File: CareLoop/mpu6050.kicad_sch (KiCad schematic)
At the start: 6 parts, among them U3 MPU-6050

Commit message: updated version
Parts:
- C11: value 10n -> 100n
- renumbered C12 to C99, JP2 to JP2_MPU2
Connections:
- net GND: now also C11.1, C13.1, C99.1; no longer C11.2, C13.2, C99.2, JP2_MPU2.1 (A)
- net at U3.13 (VDD): now also C11.2, C99.2, JP2_MPU2.1 (A), U3.8 (VLOGIC); no longer C99.1
- net at U3.20 (CPOUT): now also C13.2; no longer C13.1
- net INT renamed INT_MPU
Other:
- moved on the sheet: C11, C13, C14, C99, JP2_MPU2

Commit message: WP: update Schematics
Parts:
- C11: value 100n -> 10n
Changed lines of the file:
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@@
 	)
 	(junction
-		(at 118.11 99.06)
+		(at 161.29 109.22)
 		(diameter 0)
 		(color 0 0 0 0)
@@
 	(wire
 		(pts
+			(xy 113.03 119.38) (xy 161.29 119.38)
+		)
+		(stroke
+			(width 0)
+			(type default)
+		)
+	)
+	(wire
+		(pts
 			(xy 157.48 63.5) (xy 157.48 60.96)
 		)
@@
 	(wire
 		(pts
+			(xy 118.11 111.76) (xy 139.7 111.76)
+		)
+		(stroke
+			(width 0)
+			(type default)
+		)
+	)
+	(wire
+		(pts
+			(xy 121.92 60.96) (xy 137.16 60.96)
+		)
+		(stroke
+			(width 0)
+			(type default)
+		)
+	)
+	(wire
+		(pts
+			(xy 137.16 60.96) (xy 137.16 73.66)
+		)
+		(stroke
+			(width 0)
+			(type default)
+		)
+	)
+	(wire
+		(pts
+			(xy 167.64 109.22) (xy 167.64 111.76)
+		)
+		(stroke
+			(width 0)
+			(type default)
+		)
+	)
+	(wire
+		(pts
+			(xy 113.03 96.52) (xy 113.03 119.38)
+		)
+		(stroke
+			(width 0)
+			(type default)
+		)
+	)
+	(wire
+		(pts
+			(xy 115.57 83.82) (xy 121.92 83.82)
+		)
+		(stroke
+			(width 0)
+			(type default)
+		)
+	)
+	(wire
+		(pts
+			(xy 121.92 63.5) (xy 121.92 60.96)
+		)
+		(stroke
+			(width 0)
+			(type default)
+		)
+	)
+	(wire
+		(pts
+			(xy 172.72 96.52) (xy 172.72 101.6)
+		)
+		(stroke
+			(width 0)
+			(type default)
+		)
+	)
+	(wire
+		(pts
+			(xy 139.7 60.96) (xy 142.24 60.96)
+		)
+		(stroke
+			(width 0)
+			(type default)
+		)
+	)
+	(wire
+		(pts
+			(xy 157.48 71.12) (xy 157.48 72.39)
+		)
+		(stroke
+			(width 0)
+			(type default)
+		)
+	)
+	(wire
+		(pts
+			(xy 114.3 88.9) (xy 121.92 88.9)
+		)
+		(stroke
+			(width 0)
+			(type default)
+		)
+	)
+	(wire
+		(pts
+			(xy 161.29 99.06) (xy 157.48 99.06)
+		)
+		(stroke
+			(width 0)
+			(type default)
+		)
+	)
+	(wire
+		(pts
+			(xy 137.16 60.96) (xy 139.7 60.96)
+		)
+		(stroke
+			(width 0)
+			(type default)
+		)
+	)
+	(wire
+		(pts
+			(xy 161.29 119.38) (xy 161.29 109.22)
+		)
+		(stroke
+			(width 0)
+			(type default)
+		)
+	)
+	(wire
+		(pts
+			(xy 113.03 96.52) (xy 121.92 96.52)
+		)
+		(stroke
+			(width 0)
+			(type default)
+		)
+	)
+	(wire
+		(pts
+			(xy 118.11 99.06) (xy 121.92 99.06)
+		)
+		(stroke
+			(width 0)
+			(type default)
+		)
+	)
+	(wire
+		(pts
 			(xy 118.11 99.06) (xy 118.11 111.76)
 		)
@@
 	(wire
 		(pts
-			(xy 118.11 111.76) (xy 139.7 111.76)
-		)
-		(stroke
-			(width 0)
-			(type default)
-		)
-	)
-	(wire
-		(pts
-			(xy 121.92 60.96) (xy 137.16 60.96)
-		)
-		(stroke
-			(width 0)
-			(type default)
-		)
-	)
-	(wire
-		(pts
-			(xy 137.16 60.96) (xy 137.16 73.66)
-		)
-		(stroke
-			(width 0)
-			(type default)
-		)
-	)
-	(wire
-		(pts
-			(xy 167.64 109.22) (xy 167.64 111.76)
-		)
-		(stroke
-			(width 0)
-			(type default)
-		)
-	)
-	(wire
-		(pts
-			(xy 115.57 83.82) (xy 121.92 83.82)
-		)
-		(stroke
-			(width 0)
-			(type default)
-		)
-	)
-	(wire
-		(pts
-			(xy 121.92 63.5) (xy 121.92 60.96)
-		)
-		(stroke
-			(width 0)
-			(type default)
-		)
-	)
-	(wire
-		(pts
-			(xy 172.72 96.52) (xy 172.72 101.6)
-		)
-		(stroke
-			(width 0)
-			(type default)
-		)
-	)
-	(wire
-		(pts
-			(xy 118.11 96.52) (xy 118.11 99.06)
-		)
-		(stroke
-			(width 0)
-			(type default)
-		)
-	)
-	(wire
-		(pts
-			(xy 139.7 60.96) (xy 142.24 60.96)
-		)
-		(stroke
-			(width 0)
-			(type default)
-		)
-	)
-	(wire
-		(pts
-			(xy 157.48 71.12) (xy 157.48 72.39)
-		)
-		(stroke
-			(width 0)
-			(type default)
-		)
-	)
-	(wire
-		(pts
-			(xy 114.3 88.9) (xy 121.92 88.9)
-		)
-		(stroke
-			(width 0)
-			(type default)
-		)
-	)
-	(wire
-		(pts
-			(xy 161.29 99.06) (xy 157.48 99.06)
-		)
-		(stroke
-			(width 0)
-			(type default)
-		)
-	)
-	(wire
-		(pts
-			(xy 137.16 60.96) (xy 139.7 60.96)
-		)
-		(stroke
-			(width 0)
-			(type default)
-		)
-	)
-	(wire
-		(pts
-			(xy 118.11 99.06) (xy 121.92 99.06)
-		)
-		(stroke
-			(width 0)
-			(type default)
-		)
-	)
-	(wire
-		(pts
 			(xy 157.48 96.52) (xy 172.72 96.52)
-		)
-		(stroke
-			(width 0)
-			(type default)
-		)
-	)
-	(wire
-		(pts
-			(xy 121.92 96.52) (xy 118.11 96.52)
 		)
 		(stroke
@@
 			)
 		)
-		(property "Value" "100n"
+		(property "Value" "10n"
 			(at 125.73 68.5799 0)
 			(effects

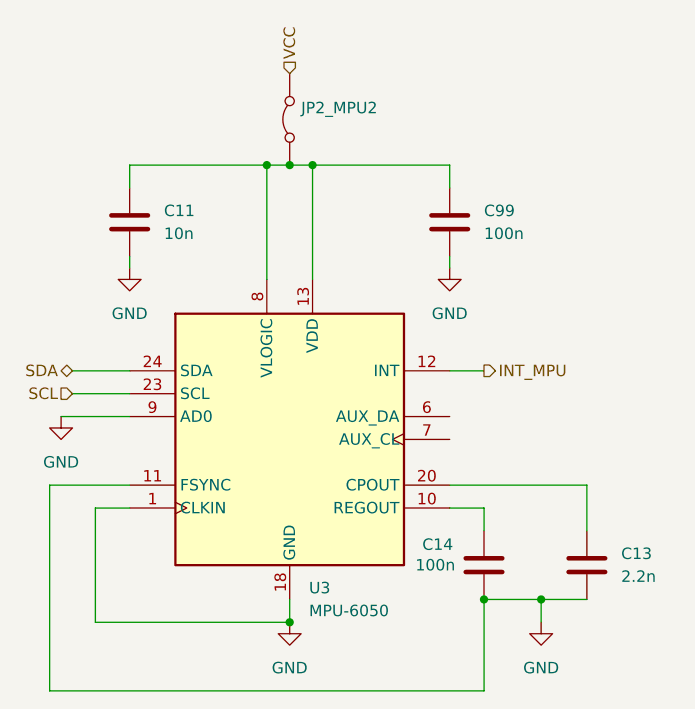
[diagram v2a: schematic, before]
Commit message: WP: Placement PCB Parts done
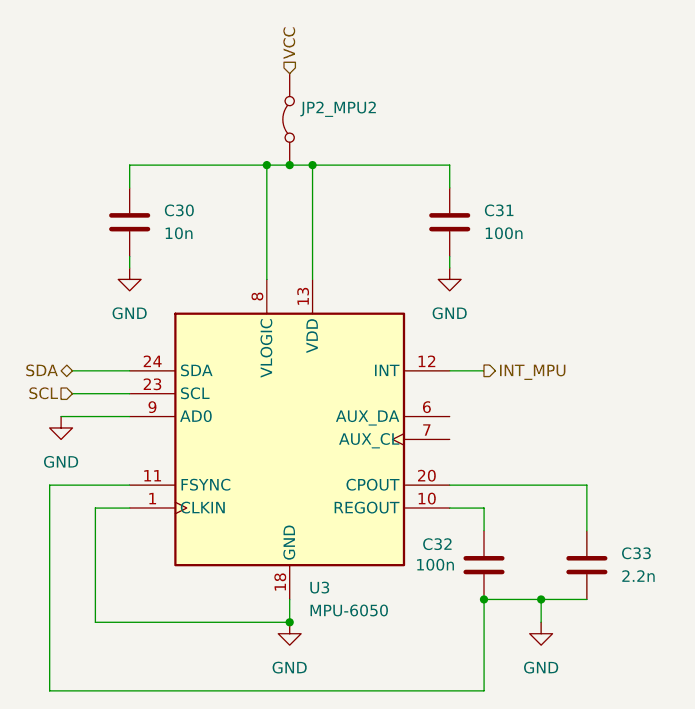
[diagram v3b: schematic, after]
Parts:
- C30: renamed from C11; footprint Capacitor_SMD:C_0603_1608Metric_Pad1.08x0.95mm_HandSolder -> Capacitor_SMD:C_0402_1005Metric_Pad0.74x0.62mm_HandSolder
- C31: renamed from C99; footprint Capacitor_SMD:C_0603_1608Metric_Pad1.08x0.95mm_HandSolder -> Capacitor_SMD:C_0201_0603Metric_Pad0.64x0.40mm_HandSolder
- C32: renamed from C14; footprint Capacitor_SMD:C_0603_1608Metric_Pad1.08x0.95mm_HandSolder -> Capacitor_SMD:C_0201_0603Metric_Pad0.64x0.40mm_HandSolder
- C33: renamed from C13; footprint Capacitor_SMD:C_0603_1608Metric_Pad1.08x0.95mm_HandSolder -> Capacitor_SMD:C_0201_0603Metric_Pad0.64x0.40mm_HandSolder
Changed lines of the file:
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@@
 		(dnp no)
 		(fields_autoplaced yes)
-		(property "Reference" "C13"
+		(property "Reference" "C33"
 			(at 176.53 104.1399 0)
 			(effects
@@
 			)
 		)
-		(property "Footprint" "Capacitor_SMD:C_0603_1608Metric_Pad1.08x0.95mm_HandSolder"
+		(property "Footprint" "Capacitor_SMD:C_0201_0603Metric_Pad0.64x0.40mm_HandSolder"
 			(at 171.7548 101.6 0)
 			(effects
@@
 			(project ""
 				(path "/1249f778-de2d-49b4-b768-08b76b87278f/2740786f-be08-4dc9-b089-426f17e30b14"
-					(reference "C13")
+					(reference "C33")
 					(unit 1)
 				)
@@
 		(dnp no)
 		(fields_autoplaced yes)
-		(property "Reference" "C11"
+		(property "Reference" "C30"
 			(at 125.73 66.0399 0)
 			(effects
@@
 			)
 		)
-		(property "Footprint" "Capacitor_SMD:C_0603_1608Metric_Pad1.08x0.95mm_HandSolder"
+		(property "Footprint" "Capacitor_SMD:C_0402_1005Metric_Pad0.74x0.62mm_HandSolder"
 			(at 120.9548 63.5 0)
 			(effects
@@
 			(project ""
 				(path "/1249f778-de2d-49b4-b768-08b76b87278f/2740786f-be08-4dc9-b089-426f17e30b14"
-					(reference "C11")
+					(reference "C30")
 					(unit 1)
 				)
@@
 		(dnp no)
 		(fields_autoplaced yes)
-		(property "Reference" "C99"
+		(property "Reference" "C31"
 			(at 161.29 66.0399 0)
 			(effects
@@
 			)
 		)
-		(property "Footprint" "Capacitor_SMD:C_0603_1608Metric_Pad1.08x0.95mm_HandSolder"
+		(property "Footprint" "Capacitor_SMD:C_0201_0603Metric_Pad0.64x0.40mm_HandSolder"
 			(at 156.5148 63.5 0)
 			(effects
@@
 			(project ""
 				(path "/1249f778-de2d-49b4-b768-08b76b87278f/2740786f-be08-4dc9-b089-426f17e30b14"
-					(reference "C99")
+					(reference "C31")
 					(unit 1)
 				)
@@
 		(on_board yes)
 		(dnp no)
-		(property "Reference" "C14"
+		(property "Reference" "C32"
 			(at 154.432 103.124 0)
 			(effects
@@
 			)
 		)
-		(property "Footprint" "Capacitor_SMD:C_0603_1608Metric_Pad1.08x0.95mm_HandSolder"
+		(property "Footprint" "Capacitor_SMD:C_0201_0603Metric_Pad0.64x0.40mm_HandSolder"
 			(at 162.2552 109.22 0)
 			(effects
@@
 			(project ""
 				(path "/1249f778-de2d-49b4-b768-08b76b87278f/2740786f-be08-4dc9-b089-426f17e30b14"
-					(reference "C14")
-					(unit 1)
-				)
+					(reference "C32")
+					(unit 1)
+				)

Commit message: update routing
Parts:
- added R5: 4k7, Resistor_SMD:R_0402_1005Metric_Pad0.72x0.64mm_HandSolder, symbol Device:R
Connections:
- net INT_MPU: now also R5.2
- net VCC: now also R5.1
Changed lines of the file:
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@@
 	(paper "A4")
+	(junction
+		(at 163.83 83.82)
+		(diameter 0)
+		(color 0 0 0 0)
+	)
 	(junction
 		(at 137.16 60.96)
@@
 	(wire
 		(pts
-			(xy 157.48 83.82) (xy 161.29 83.82)
+			(xy 157.48 83.82) (xy 163.83 83.82)
+		)
+		(stroke
+			(width 0)
+			(type default)
+		)
+	)
+	(wire
+		(pts
+			(xy 163.83 83.82) (xy 168.91 83.82)
 		)
 		(stroke
@@
 	(wire
 		(pts
+			(xy 163.83 82.55) (xy 163.83 83.82)
+		)
+		(stroke
+			(width 0)
+			(type default)
+		)
+	)
+	(wire
+		(pts
+			(xy 163.83 71.12) (xy 168.91 71.12)
+		)
+		(stroke
+			(width 0)
+			(type default)
+		)
+	)
+	(wire
+		(pts
 			(xy 115.57 83.82) (xy 121.92 83.82)
 		)
@@
 		(pts
 			(xy 172.72 96.52) (xy 172.72 101.6)
+		)
+		(stroke
+			(width 0)
+			(type default)
+		)
+	)
+	(wire
+		(pts
+			(xy 163.83 74.93) (xy 163.83 71.12)
 		)
 		(stroke
@@
 	(hierarchical_label "INT_MPU"
 		(shape output)
-		(at 161.29 83.82 0)
+		(at 168.91 83.82 0)
 		(effects
 			(font
@@
 		(shape input)
 		(at 139.7 50.8 90)
+		(effects
+			(font
+				(size 1.27 1.27)
+			)
+			(justify left)
+		)
+	)
+	(hierarchical_label "VCC"
+		(shape input)
+		(at 168.91 71.12 0)
 		(effects
 			(font
@@
 					(unit 1)
 				)
+			)
+		)
+	)
+	(symbol
+		(lib_id "Device:R")
+		(at 163.83 78.74 0)
+		(unit 1)
+		(exclude_from_sim no)
+		(in_bom yes)
+		(on_board yes)
+		(dnp no)
+		(fields_autoplaced yes)
+		(property "Reference" "R5"
+			(at 166.37 77.4699 0)
+			(effects
+				(font
+					(size 1.27 1.27)
+				)
+				(justify left)
+			)
+		)
+		(property "Value" "4k7"
+			(at 166.37 80.0099 0)
+			(effects
+				(font
+					(size 1.27 1.27)
+				)
+				(justify left)
+			)
+		)
+		(property "Footprint" "Resistor_SMD:R_0402_1005Metric_Pad0.72x0.64mm_HandSolder"
+			(at 162.052 78.74 90)
+			(effects
+				(font
+					(size 1.27 1.27)
+				)
+				(hide yes)
+			)
+		)
+		(property "Datasheet" "~"
+			(at 163.83 78.74 0)
+			(effects
+				(font
+					(size 1.27 1.27)
+				)
+				(hide yes)
+			)
+		)
+		(property "Description" "Resistor"
+			(at 163.83 78.74 0)
+			(effects
+				(font
+					(size 1.27 1.27)
+				)
+				(hide yes)
+			)
+		)
+		(pin "2"
+		)
+		(pin "1"
+		)
+		(instances
+			(project ""
+				(path "/1249f778-de2d-49b4-b768-08b76b87278f/2740786f-be08-4dc9-b089-426f17e30b14"
+					(reference "R5")
+					(unit 1)
+				)

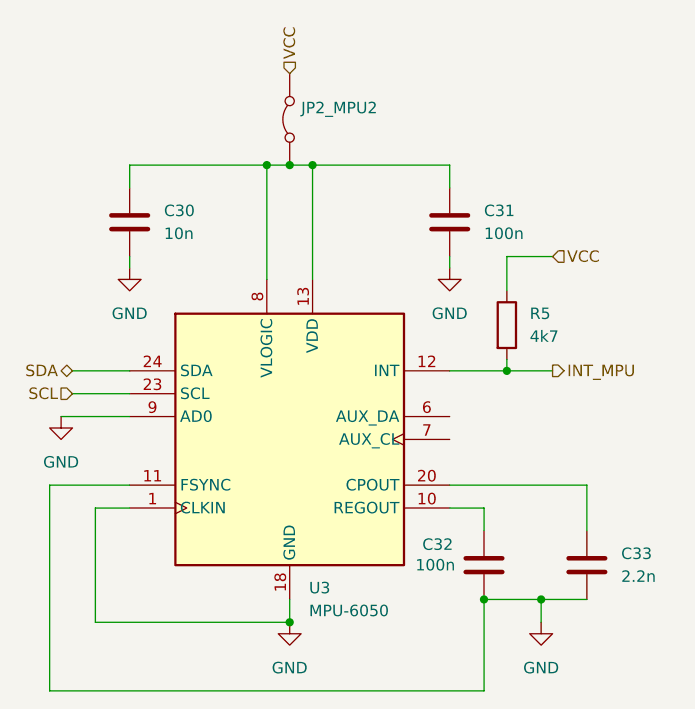
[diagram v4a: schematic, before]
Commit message: updated vias
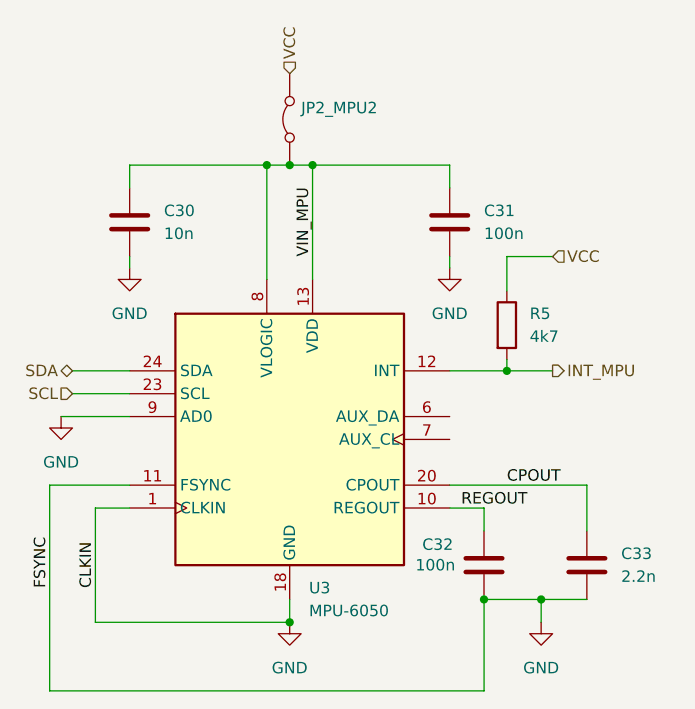
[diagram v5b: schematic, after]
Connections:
- net REGOUT: now reaches C32.1, U3.10 (REGOUT)
- net VIN_MPU: now reaches C30.2, C31.2, JP2_MPU2.1 (A), U3.13 (VDD), U3.8 (VLOGIC)
- net CPOUT: now reaches C33.2, U3.20 (CPOUT)
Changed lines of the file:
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@@
+		)
+	)
+	(label "CPOUT"
+		(at 163.83 96.52 0)
+		(effects
+			(font
+				(size 1.27 1.27)
+			)
+			(justify left bottom)
+		)
+	)
+	(label "FSYNC"
+		(at 113.03 107.95 90)
+		(effects
+			(font
+				(size 1.27 1.27)
+			)
+			(justify left bottom)
+		)
+	)
+	(label "CLKIN"
+		(at 118.11 107.95 90)
+		(effects
+			(font
+				(size 1.27 1.27)
+			)
+			(justify left bottom)
+		)
+	)
+	(label "REGOUT"
+		(at 158.75 99.06 0)
+		(effects
+			(font
+				(size 1.27 1.27)
+			)
+			(justify left bottom)
+		)
+	)
+	(label "VIN_MPU"
+		(at 142.24 71.12 90)
+		(effects
+			(font
+				(size 1.27 1.27)
+			)
+			(justify left bottom)
 		)
 	)

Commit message: update PCB
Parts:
- C30: JLCPCB Part#(optional) (none) -> C1524
- C31, C32: JLCPCB Part#(optional) (none) -> C161494
- C33: JLCPCB Part#(optional) (none) -> C80433
- JP2_MPU2: footprint Connector_PinHeader_1.00mm:PinHeader_1x02_P1.00mm_Vertical -> Connector_PinHeader_2.00mm:PinHeader_1x02_P2.00mm_Vertical; now not fitted
- R5: JLCPCB Part#(optional) (none) -> C22369185
- U3: JLCPCB Part#(optional) (none) -> C24112
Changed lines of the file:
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@@
+			)
+		)
+		(property "JLCPCB Part#(optional)" "C24112"
+			(at 139.7 91.44 0)
+			(effects
+				(font
+					(size 1.27 1.27)
+				)
+				(hide yes)
 			)
 		)
@@
 			)
 		)
+		(property "JLCPCB Part#(optional)" "C80433"
+			(at 172.72 105.41 0)
+			(effects
+				(font
+					(size 1.27 1.27)
+				)
+				(hide yes)
+			)
+		)
 		(pin "1"
 		)
@@
 			)
 		)
+		(property "JLCPCB Part#(optional)" "C1524"
+			(at 121.92 67.31 0)
+			(effects
+				(font
+					(size 1.27 1.27)
+				)
+				(hide yes)
+			)
+		)
 		(pin "1"
 		)
@@
 		(in_bom yes)
 		(on_board yes)
-		(dnp no)
+		(dnp yes)
 		(fields_autoplaced yes)
 		(property "Reference" "JP2_MPU2"
@@
 			)
 		)
-		(property "Footprint" "Connector_PinHeader_1.00mm:PinHeader_1x02_P1.00mm_Vertical"
+		(property "Footprint" "Connector_PinHeader_2.00mm:PinHeader_1x02_P2.00mm_Vertical"
 			(at 139.7 55.88 0)
 			(effects
@@
 			)
 		)
+		(property "JLCPCB Part#(optional)" ""
+			(at 139.7 55.88 90)
+			(effects
+				(font
+					(size 1.27 1.27)
+				)
+				(hide yes)
+			)
+		)
 		(pin "2"
 		)
@@
 			)
 		)
+		(property "JLCPCB Part#(optional)" "C161494"
+			(at 157.48 67.31 0)
+			(effects
+				(font
+					(size 1.27 1.27)
+				)
+				(hide yes)
+			)
+		)
 		(pin "1"
 		)
@@
 			)
 		)
+		(property "JLCPCB Part#(optional)" "C22369185"
+			(at 163.83 78.74 0)
+			(effects
+				(font
+					(size 1.27 1.27)
+				)
+				(hide yes)
+			)
+		)
 		(pin "2"
 		)
@@
 			(at 161.29 105.41 0)
 			(effects
+				(font
+					(size 1.27 1.27)
+				)
+				(hide yes)
+			)
+		)
+		(property "JLCPCB Part#(optional)" "C161494"
+			(at 161.29 105.41 0)
+			(effects

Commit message: nordic review
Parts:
- C31, C32: JLCPCB Part#(optional) C161494 -> C161404
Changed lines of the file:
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@@
 			)
 		)
-		(property "JLCPCB Part#(optional)" "C161494"
+		(property "JLCPCB Part#(optional)" "C161404"
 			(at 157.48 67.31 0)
 			(effects
@@
 			)
 		)
-		(property "JLCPCB Part#(optional)" "C161494"
+		(property "JLCPCB Part#(optional)" "C161404"
 			(at 161.29 105.41 0)
 			(effects
